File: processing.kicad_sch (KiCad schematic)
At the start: 20 parts, among them SW1 SW_Push, SW2 SW_Push, U4 ESP32-WROOM-32E, U5 BME280

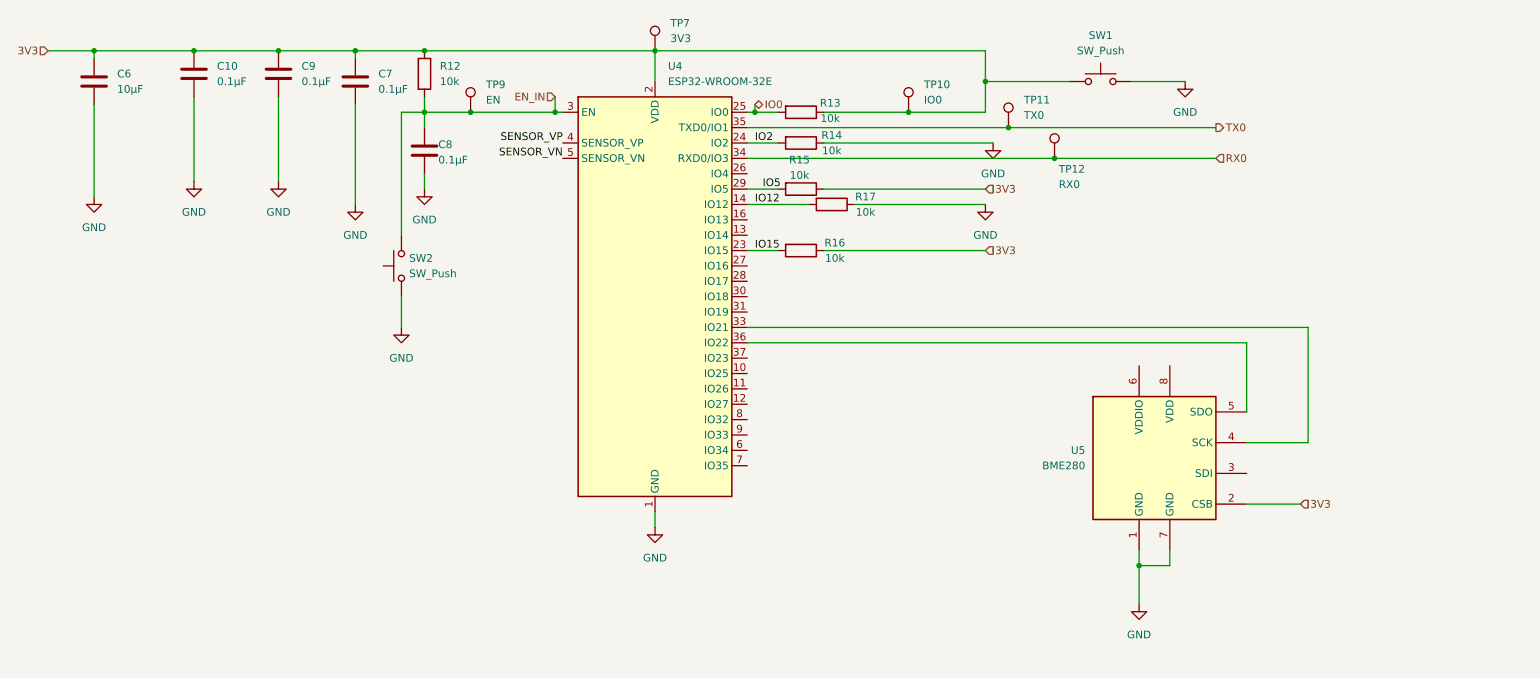
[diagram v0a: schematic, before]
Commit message: completed the sensor node core (esp32 and the sensor chip)
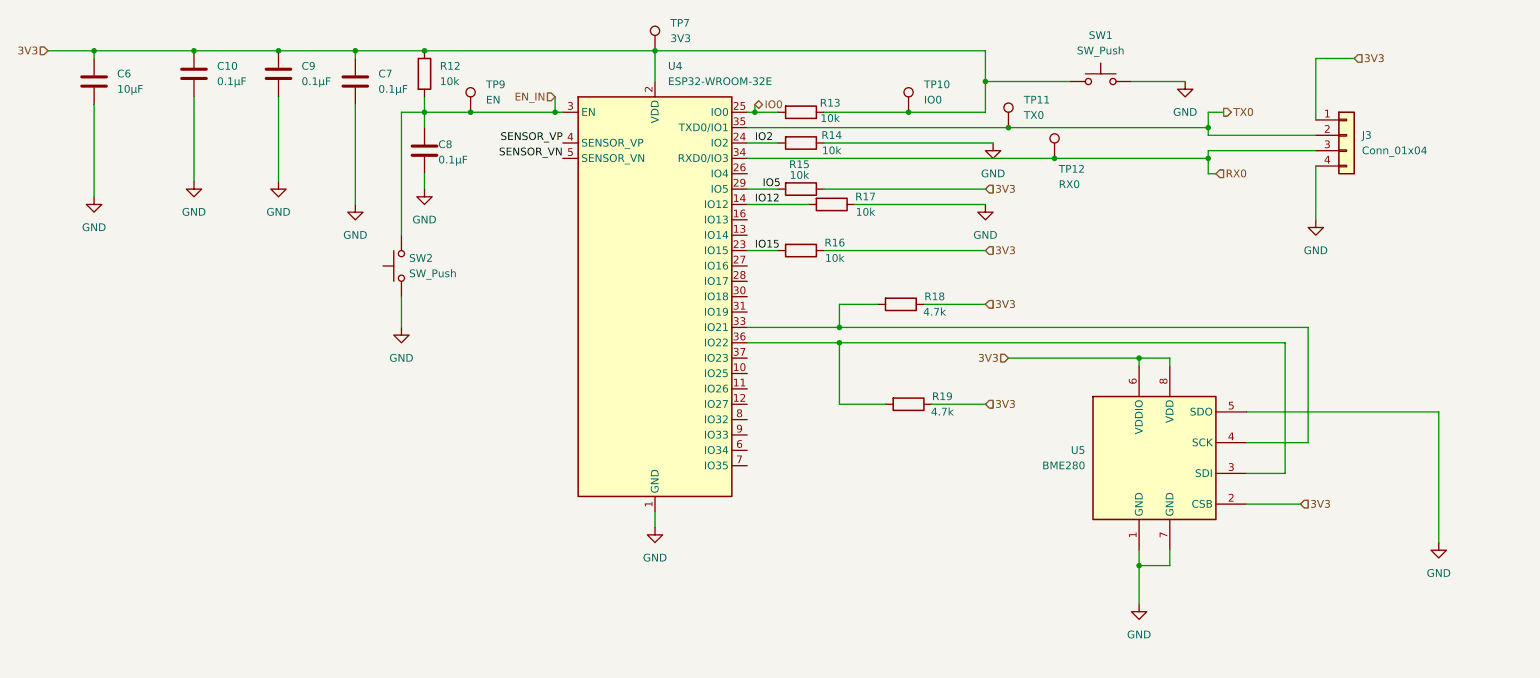
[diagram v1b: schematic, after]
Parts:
- added J3: Conn_01x04, symbol Connector_Generic:Conn_01x04
- added R18, R19: 4.7k, Resistor_SMD:R_0603_1608Metric, symbol Device:R
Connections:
- net 3V3: now also U5.6 (VDDIO), U5.8 (VDD), J3.1 (Pin_1), R18.1, R19.1
- net GND: now also U5.5 (SDO), J3.4 (Pin_4)
- net RX0: now also J3.3 (Pin_3)
- net TX0: now also J3.2 (Pin_2)
- net at U5.3 (SDI): now also U4.36 (IO22), R19.2
- net at U4.33 (IO21), U5.4 (SCK): now also R18.2

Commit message: finalized the schematic design
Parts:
- added C11: 0.1µF, Capacitor_SMD:C_0603_1608Metric, symbol Device:C
- added R20, R21: 100k, Resistor_SMD:R_0603_1608Metric, symbol Device:R
- J3: footprint (none) -> Connector_PinHeader_2.54mm:PinHeader_1x04_P2.54mm_Vertical
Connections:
- net 3V3: now also C11.1
- net GND: now also C11.2, R20.2
- net at U4.7 (IO35): now also R21.1
- net EN_IN: no longer names the net of C8.1, R12.2, SW2.2, TP9.1, U4.3 (EN)
- net IO0: no longer names the net of R13.2, U4.25 (IO0)
- net RX0: no longer names the net of J3.3 (Pin_3), TP12.1, U4.34 (RXD0/IO3)
- net SENSOR_VN: no longer names the net of U4.5 (SENSOR_VN)
- net SENSOR_VP: no longer names the net of U4.4 (SENSOR_VP)
- net TX0: no longer names the net of J3.2 (Pin_2), TP11.1, U4.35 (TXD0/IO1)
- new net BATT+: R20.1, R21.2
- no-connect marks 0 -> 16
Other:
- title: (none) -> Sensor Node Core
